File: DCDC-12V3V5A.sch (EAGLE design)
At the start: 37 parts, among them Q10 NMOSFET, Q9 NMOSFET, U1 LM3150MHX/NOPB

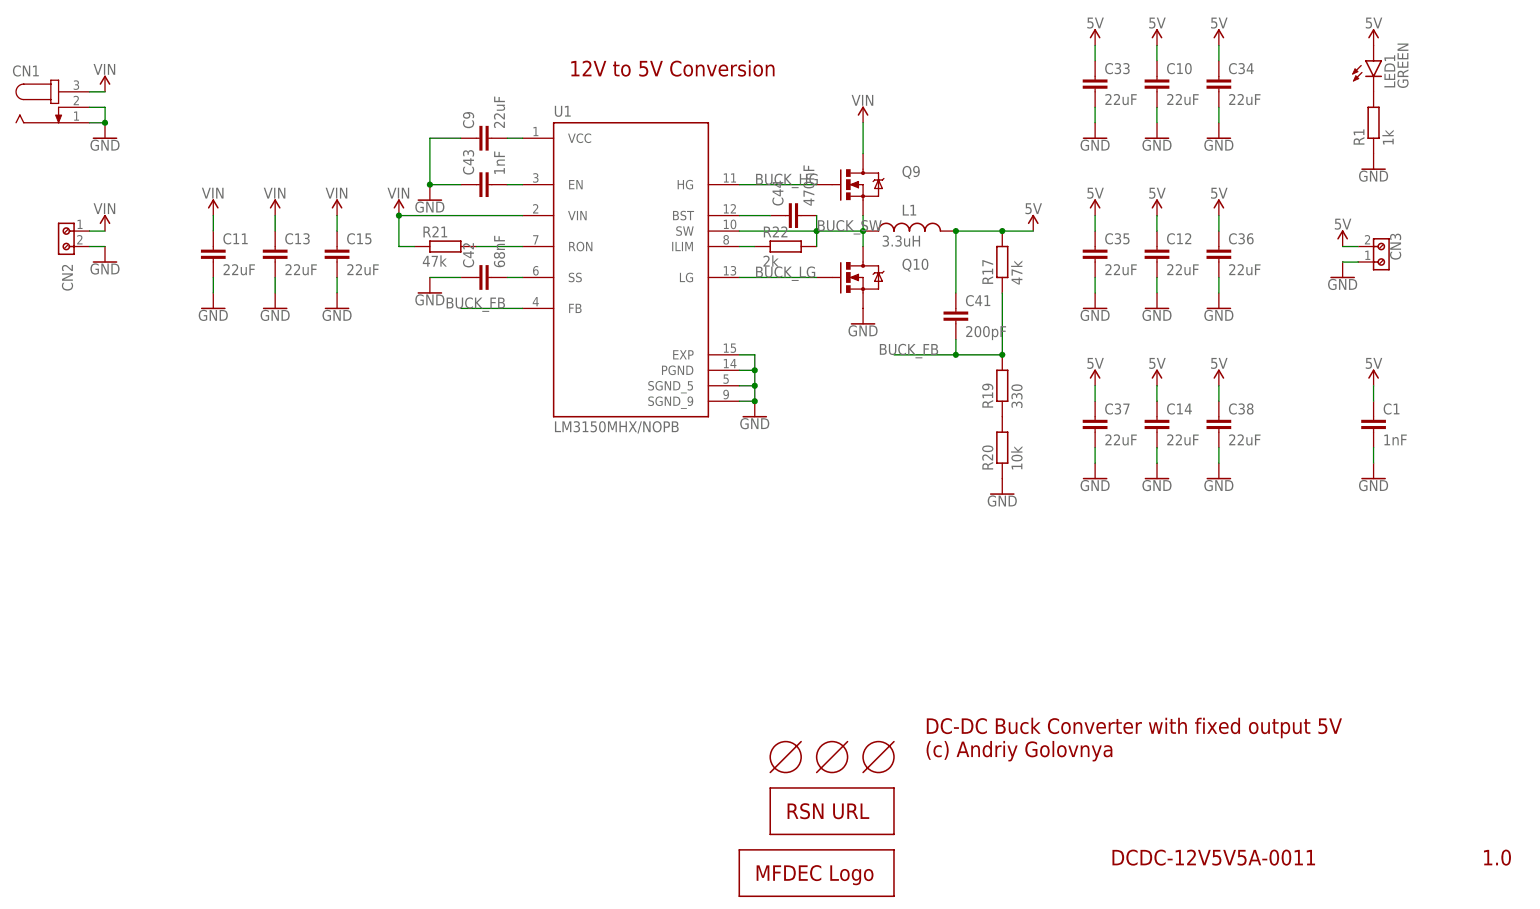
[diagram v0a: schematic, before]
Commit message: Fixed text on schematics. Generated PDF schematics. Removed wrongly committed CSV file.
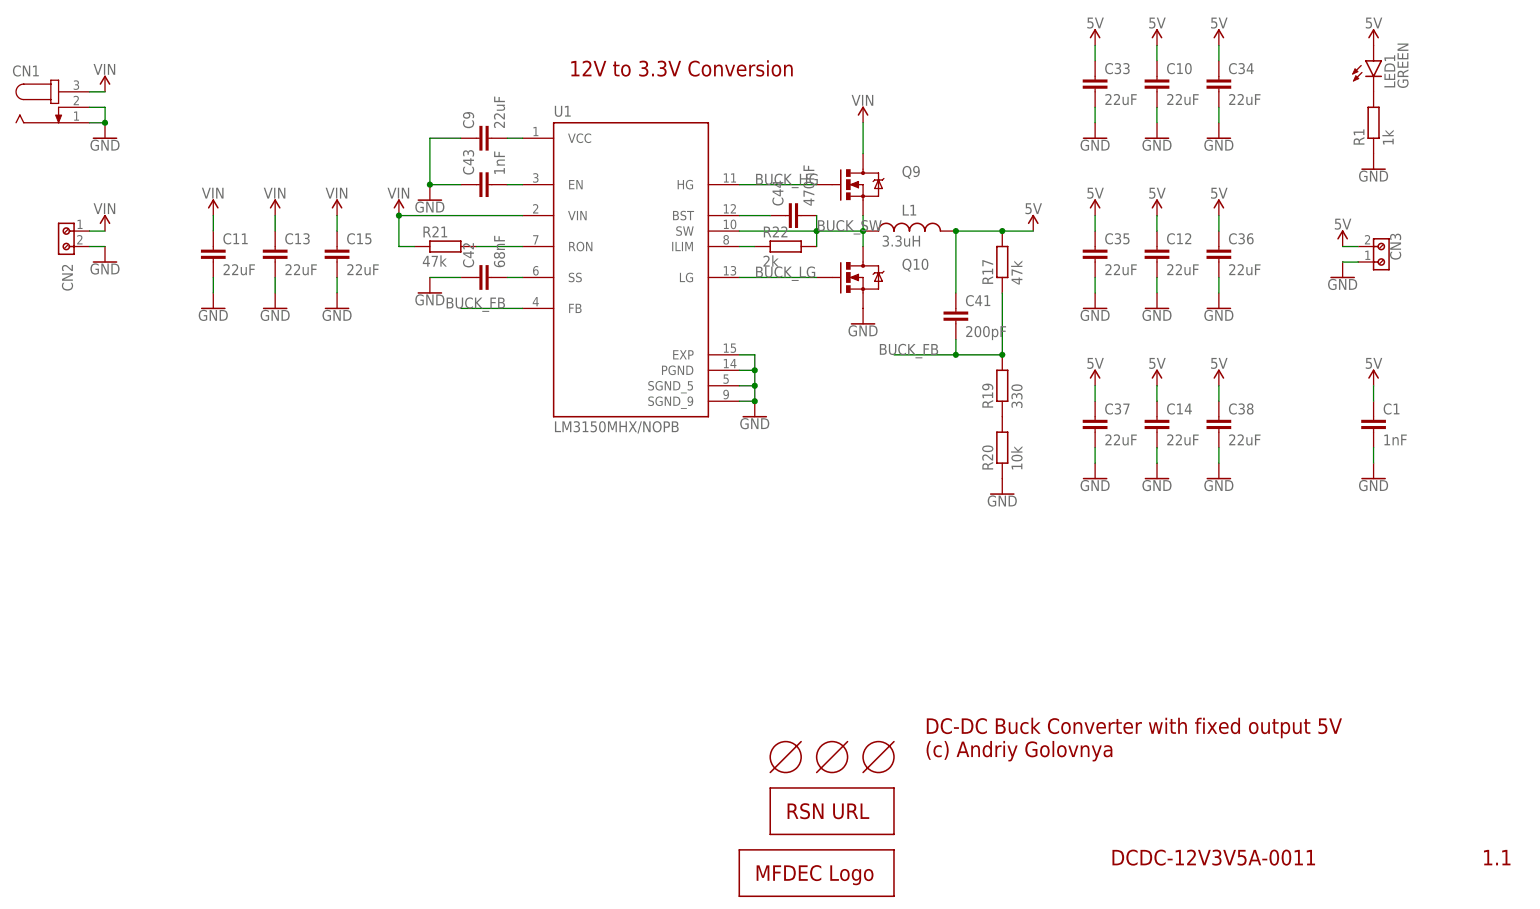
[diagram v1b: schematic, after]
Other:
- note added: "1.1"
- note added: "12V to 3.3V Conversion"
- note added: "DCDC-12V3V5A-0011"
- note removed: "1.0"
- note removed: "12V to 5V Conversion"
- note removed: "DCDC-12V5V5A-0011"
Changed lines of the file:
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@@
 <sheet>
 <plain>
-<text x="256.54" y="7.62" size="2.54" layer="94">1.0</text>
-<text x="195.58" y="7.62" size="2.54" layer="94">DCDC-12V5V5A-0011</text>
+<text x="256.54" y="7.62" size="2.54" layer="94">1.1</text>
+<text x="195.58" y="7.62" size="2.54" layer="94">DCDC-12V3V5A-0011</text>
 <text x="165.1" y="25.4" size="2.54" layer="94">DC-DC Buck Converter with fixed output 5V
 (c) Andriy Golovnya</text>
-<text x="106.68" y="137.16" size="2.54" layer="94">12V to 5V Conversion</text>
+<text x="106.68" y="137.16" size="2.54" layer="94">12V to 3.3V Conversion</text>
 </plain>
 <instances>

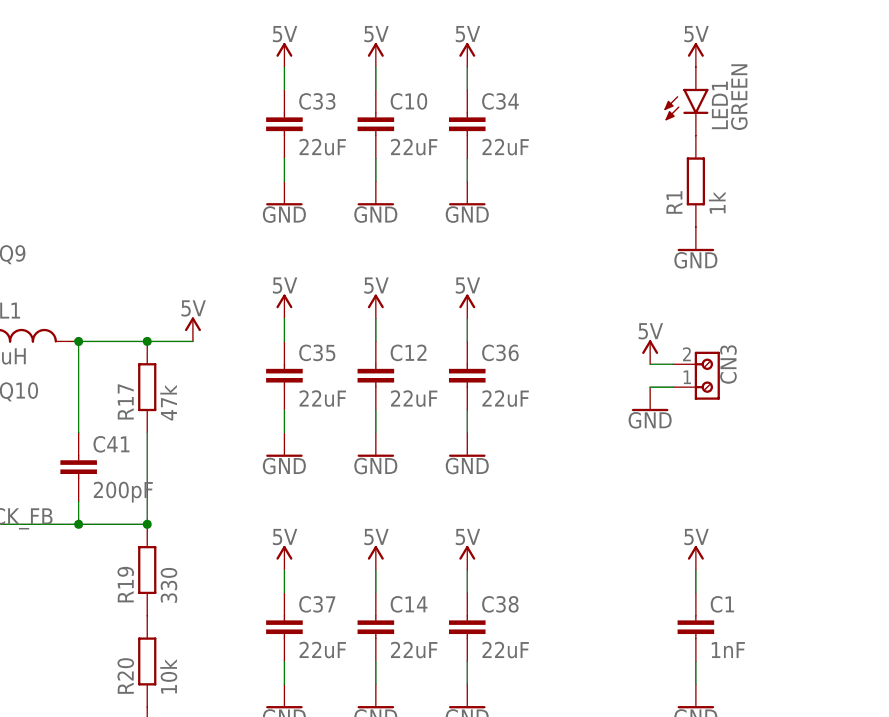
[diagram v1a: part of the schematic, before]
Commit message: Added proper voltage symbols on 3.3v and 12v boards. Generated PDF schematics.
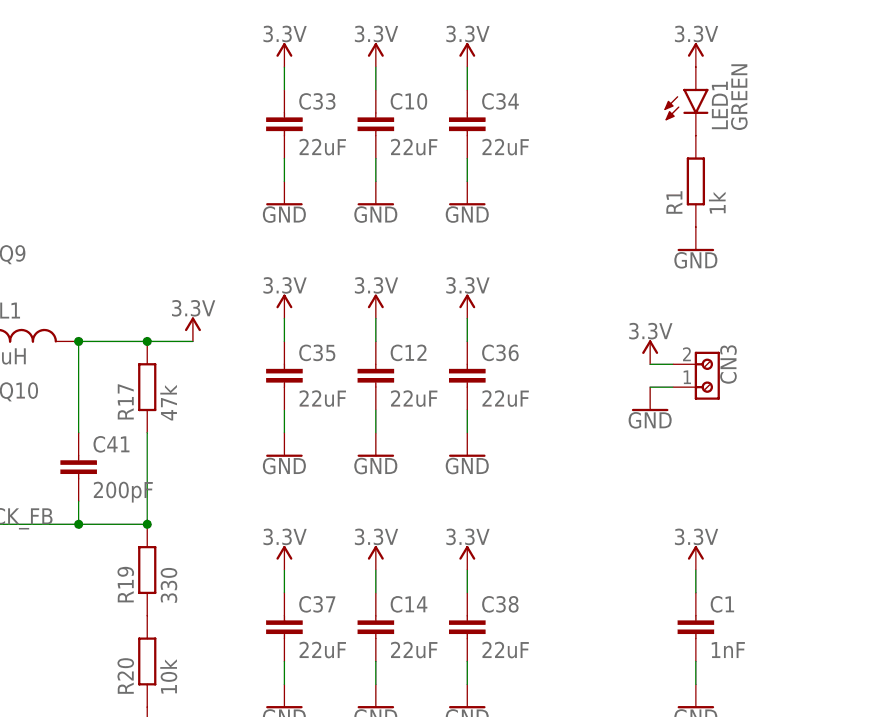
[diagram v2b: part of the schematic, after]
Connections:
- net 5V renamed 3.3V
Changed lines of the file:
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@@
 <part name="C37" library="rcl" library_urn="urn:adsk.eagle:library:334" deviceset="C-EU" device="C0805K" package3d_urn="urn:adsk.eagle:package:23681/2" value="22uF"/>
 <part name="C38" library="rcl" library_urn="urn:adsk.eagle:library:334" deviceset="C-EU" device="C0805K" package3d_urn="urn:adsk.eagle:package:23681/2" value="22uF"/>
-<part name="SUPPLY41" library="SparkFun-PowerSymbols" library_urn="urn:adsk.eagle:library:530" deviceset="5V" device=""/>
-<part name="SUPPLY42" library="SparkFun-PowerSymbols" library_urn="urn:adsk.eagle:library:530" deviceset="5V" device=""/>
-<part name="SUPPLY43" library="SparkFun-PowerSymbols" library_urn="urn:adsk.eagle:library:530" deviceset="5V" device=""/>
+<part name="SUPPLY41" library="SparkFun-PowerSymbols" library_urn="urn:adsk.eagle:library:530" deviceset="3.3V" device=""/>
+<part name="SUPPLY42" library="SparkFun-PowerSymbols" library_urn="urn:adsk.eagle:library:530" deviceset="3.3V" device=""/>
+<part name="SUPPLY43" library="SparkFun-PowerSymbols" library_urn="urn:adsk.eagle:library:530" deviceset="3.3V" device=""/>
 <part name="U1" library="LM3150MHX_NOPB" deviceset="LM3150MHX/NOPB" device=""/>
 <part name="Q9" library="BeagleBone_Blue_R3" library_urn="urn:adsk.eagle:library:5828899" deviceset="MOSFET-NCHANNEL" device="FDD8780" package3d_urn="urn:adsk.eagle:package:5829549/1" value="NMOSFET"/>
@@
 <part name="GND51" library="SparkFun-PowerSymbols" library_urn="urn:adsk.eagle:library:530" deviceset="GND" device=""/>
 <part name="L1" library="Wurth_Automotive_WE-CHSA" library_urn="urn:adsk.eagle:library:14076700" deviceset="WE-CHSA_1011" device="" package3d_urn="urn:adsk.eagle:package:13154812/4" technology="_7843330330" value="3.3uH"/>
-<part name="SUPPLY45" library="SparkFun-PowerSymbols" library_urn="urn:adsk.eagle:library:530" deviceset="5V" device=""/>
+<part name="SUPPLY45" library="SparkFun-PowerSymbols" library_urn="urn:adsk.eagle:library:530" deviceset="3.3V" device=""/>
 <part name="GND52" library="SparkFun-PowerSymbols" library_urn="urn:adsk.eagle:library:530" deviceset="GND" device=""/>
 <part name="SUPPLY46" library="SparkFun-PowerSymbols" library_urn="urn:adsk.eagle:library:530" deviceset="VIN" device=""/>
@@
 <part name="SUPPLY3" library="SparkFun-PowerSymbols" library_urn="urn:adsk.eagle:library:530" deviceset="VIN" device=""/>
 <part name="SUPPLY5" library="SparkFun-PowerSymbols" library_urn="urn:adsk.eagle:library:530" deviceset="VIN" device=""/>
-<part name="SUPPLY8" library="SparkFun-PowerSymbols" library_urn="urn:adsk.eagle:library:530" deviceset="5V" device=""/>
-<part name="SUPPLY47" library="SparkFun-PowerSymbols" library_urn="urn:adsk.eagle:library:530" deviceset="5V" device=""/>
-<part name="SUPPLY48" library="SparkFun-PowerSymbols" library_urn="urn:adsk.eagle:library:530" deviceset="5V" device=""/>
-<part name="SUPPLY49" library="SparkFun-PowerSymbols" library_urn="urn:adsk.eagle:library:530" deviceset="5V" device=""/>
-<part name="SUPPLY50" library="SparkFun-PowerSymbols" library_urn="urn:adsk.eagle:library:530" deviceset="5V" device=""/>
-<part name="SUPPLY51" library="SparkFun-PowerSymbols" library_urn="urn:adsk.eagle:library:530" deviceset="5V" device=""/>
+<part name="SUPPLY8" library="SparkFun-PowerSymbols" library_urn="urn:adsk.eagle:library:530" deviceset="3.3V" device=""/>
+<part name="SUPPLY47" library="SparkFun-PowerSymbols" library_urn="urn:adsk.eagle:library:530" deviceset="3.3V" device=""/>
+<part name="SUPPLY48" library="SparkFun-PowerSymbols" library_urn="urn:adsk.eagle:library:530" deviceset="3.3V" device=""/>
+<part name="SUPPLY49" library="SparkFun-PowerSymbols" library_urn="urn:adsk.eagle:library:530" deviceset="3.3V" device=""/>
+<part name="SUPPLY50" library="SparkFun-PowerSymbols" library_urn="urn:adsk.eagle:library:530" deviceset="3.3V" device=""/>
+<part name="SUPPLY51" library="SparkFun-PowerSymbols" library_urn="urn:adsk.eagle:library:530" deviceset="3.3V" device=""/>
 <part name="GND58" library="SparkFun-PowerSymbols" library_urn="urn:adsk.eagle:library:530" deviceset="GND" device=""/>
 <part name="GND59" library="SparkFun-PowerSymbols" library_urn="urn:adsk.eagle:library:530" deviceset="GND" device=""/>
@@
 <part name="SUPPLY1" library="SparkFun-PowerSymbols" library_urn="urn:adsk.eagle:library:530" deviceset="VIN" device=""/>
 <part name="GND3" library="SparkFun-PowerSymbols" library_urn="urn:adsk.eagle:library:530" deviceset="GND" device=""/>
-<part name="SUPPLY6" library="SparkFun-PowerSymbols" library_urn="urn:adsk.eagle:library:530" deviceset="5V" device=""/>
+<part name="SUPPLY6" library="SparkFun-PowerSymbols" library_urn="urn:adsk.eagle:library:530" deviceset="3.3V" device=""/>
 <part name="LOGO1" library="_my_logos" deviceset="RSNURL" device="_QR_8MM" value="RSNURL_QR_8MM"/>
 <part name="LOGO2" library="_my_logos" deviceset="MFDECLOGO" device="_L_10MM" value="MFDECLOGO_L_10MM"/>
 <part name="LED1" library="led" library_urn="urn:adsk.eagle:library:259" deviceset="LED" device="SML0603" package3d_urn="urn:adsk.eagle:package:15832/1" value="GREEN"/>
 <part name="R1" library="rcl" library_urn="urn:adsk.eagle:library:334" deviceset="R-EU_" device="R0603" package3d_urn="urn:adsk.eagle:package:23555/3" value="1k"/>
-<part name="SUPPLY7" library="SparkFun-PowerSymbols" library_urn="urn:adsk.eagle:library:530" deviceset="5V" device=""/>
+<part name="SUPPLY7" library="SparkFun-PowerSymbols" library_urn="urn:adsk.eagle:library:530" deviceset="3.3V" device=""/>
 <part name="GND4" library="SparkFun-PowerSymbols" library_urn="urn:adsk.eagle:library:530" deviceset="GND" device=""/>
 <part name="HOLE1" library="_my_fiducia" deviceset="TOOLINGHOLE" device=""/>
@@
 <part name="HOLE3" library="_my_fiducia" deviceset="TOOLINGHOLE" device=""/>
 <part name="C1" library="rcl" library_urn="urn:adsk.eagle:library:334" deviceset="C-EU" device="C0603K" package3d_urn="urn:adsk.eagle:package:23680/2" value="1nF"/>
-<part name="SUPPLY9" library="SparkFun-PowerSymbols" library_urn="urn:adsk.eagle:library:530" deviceset="5V" device=""/>
+<part name="SUPPLY9" library="SparkFun-PowerSymbols" library_urn="urn:adsk.eagle:library:530" deviceset="3.3V" device=""/>
 <part name="GND5" library="SparkFun-PowerSymbols" library_urn="urn:adsk.eagle:library:530" deviceset="GND" device=""/>
 <part name="SUPPLY4" library="SparkFun-PowerSymbols" library_urn="urn:adsk.eagle:library:530" deviceset="VIN" device=""/>
@@
 </segment>
 </net>
-<net name="5V" class="0">
+<net name="3.3V" class="0">
 <segment>
 <pinref part="C34" gate="G$1" pin="1"/>
 <wire x1="213.36" y1="139.7" x2="213.36" y2="142.24" width="0.1524" layer="91"/>
-<pinref part="SUPPLY43" gate="G$1" pin="5V"/>
+<pinref part="SUPPLY43" gate="G$1" pin="3.3V"/>
 </segment>
 <segment>
 <pinref part="C36" gate="G$1" pin="1"/>
 <wire x1="213.36" y1="111.76" x2="213.36" y2="114.3" width="0.1524" layer="91"/>
-<pinref part="SUPPLY42" gate="G$1" pin="5V"/>
+<pinref part="SUPPLY42" gate="G$1" pin="3.3V"/>
 </segment>
 <segment>
 <pinref part="C38" gate="G$1" pin="1"/>
 <wire x1="213.36" y1="83.82" x2="213.36" y2="86.36" width="0.1524" layer="91"/>
-<pinref part="SUPPLY41" gate="G$1" pin="5V"/>
+<pinref part="SUPPLY41" gate="G$1" pin="3.3V"/>
 </segment>
 <segment>
 <pinref part="L1" gate="G$1" pin="2"/>
-<pinref part="SUPPLY45" gate="G$1" pin="5V"/>
+<pinref part="SUPPLY45" gate="G$1" pin="3.3V"/>
 <pinref part="R17" gate="G$1" pin="2"/>
 <wire x1="170.18" y1="111.76" x2="177.8" y2="111.76" width="0.1524" layer="91"/>
@@
 <pinref part="C10" gate="G$1" pin="1"/>
 <wire x1="203.2" y1="142.24" x2="203.2" y2="139.7" width="0.1524" layer="91"/>
-<pinref part="SUPPLY8" gate="G$1" pin="5V"/>
+<pinref part="SUPPLY8" gate="G$1" pin="3.3V"/>
 </segment>
 <segment>
 <pinref part="C33" gate="G$1" pin="1"/>
 <wire x1="193.04" y1="142.24" x2="193.04" y2="139.7" width="0.1524" layer="91"/>
-<pinref part="SUPPLY47" gate="G$1" pin="5V"/>
+<pinref part="SUPPLY47" gate="G$1" pin="3.3V"/>
 </segment>
 <segment>
 <pinref part="C12" gate="G$1" pin="1"/>
 <wire x1="203.2" y1="114.3" x2="203.2" y2="111.76" width="0.1524" layer="91"/>
-<pinref part="SUPPLY48" gate="G$1" pin="5V"/>
+<pinref part="SUPPLY48" gate="G$1" pin="3.3V"/>
 </segment>
 <segment>
 <pinref part="C35" gate="G$1" pin="1"/>
 <wire x1="193.04" y1="114.3" x2="193.04" y2="111.76" width="0.1524" layer="91"/>
-<pinref part="SUPPLY49" gate="G$1" pin="5V"/>
+<pinref part="SUPPLY49" gate="G$1" pin="3.3V"/>
 </segment>
 <segment>
 <pinref part="C14" gate="G$1" pin="1"/>
 <wire x1="203.2" y1="86.36" x2="203.2" y2="83.82" width="0.1524" layer="91"/>
-<pinref part="SUPPLY50" gate="G$1" pin="5V"/>
+<pinref part="SUPPLY50" gate="G$1" pin="3.3V"/>
 </segment>
 <segment>
 <pinref part="C37" gate="G$1" pin="1"/>
 <wire x1="193.04" y1="86.36" x2="193.04" y2="83.82" width="0.1524" layer="91"/>
-<pinref part="SUPPLY51" gate="G$1" pin="5V"/>
-</segment>
-<segment>
-<pinref part="SUPPLY6" gate="G$1" pin="5V"/>
+<pinref part="SUPPLY51" gate="G$1" pin="3.3V"/>
+</segment>
+<segment>
+<pinref part="SUPPLY6" gate="G$1" pin="3.3V"/>
 <pinref part="CN3" gate="G$1" pin="2"/>
 <wire x1="233.68" y1="109.22" x2="236.22" y2="109.22" width="0.1524" layer="91"/>
@@
 <segment>
 <pinref part="LED1" gate="G$1" pin="A"/>
-<pinref part="SUPPLY7" gate="G$1" pin="5V"/>
+<pinref part="SUPPLY7" gate="G$1" pin="3.3V"/>
 </segment>
 <segment>
 <pinref part="C1" gate="G$1" pin="1"/>
-<pinref part="SUPPLY9" gate="G$1" pin="5V"/>
+<pinref part="SUPPLY9" gate="G$1" pin="3.3V"/>
 <wire x1="238.76" y1="83.82" x2="238.76" y2="86.36" width="0.1524" layer="91"/>
 </segment>

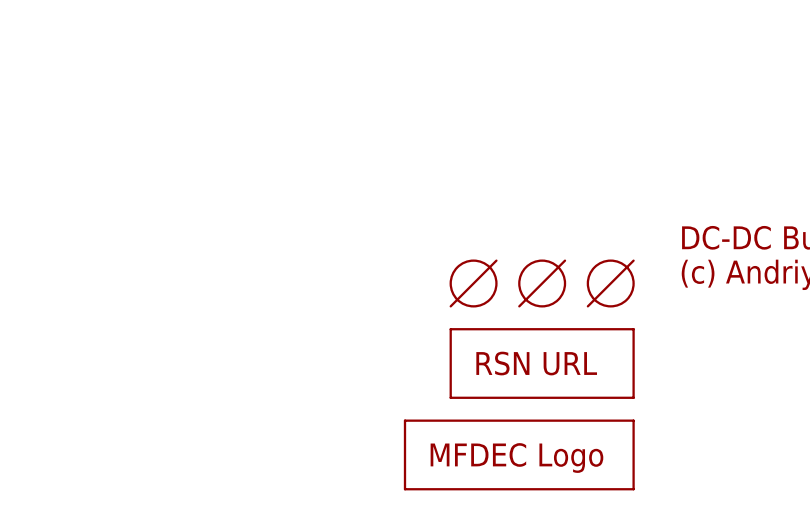
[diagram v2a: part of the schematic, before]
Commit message: Moved some texts and tooling holes a bit. Generated CAM files. Generated PNG preview. Generated PDF schematics. Renamed BoM and PnP files.
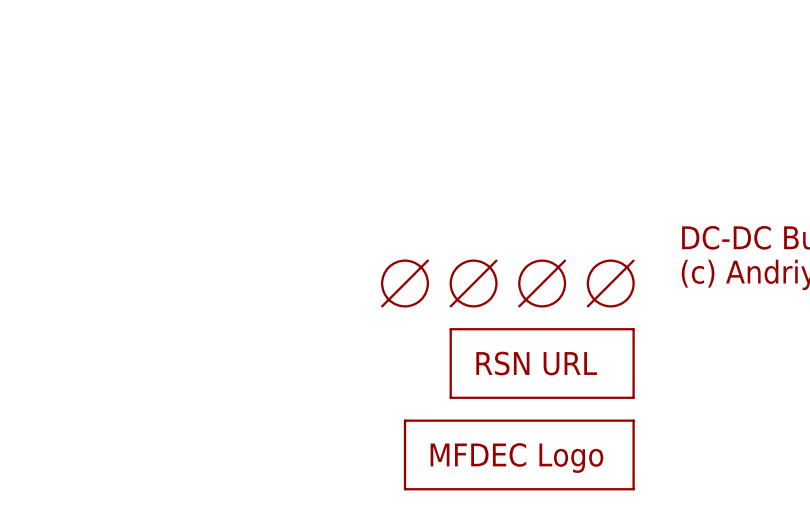
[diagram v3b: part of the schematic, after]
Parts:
- added HOLE4: TOOLINGHOLE, _my_fiducia:TOOLINGHOLE
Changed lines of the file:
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@@
 <part name="SUPPLY4" library="SparkFun-PowerSymbols" library_urn="urn:adsk.eagle:library:530" deviceset="VIN" device=""/>
 <part name="GND1" library="SparkFun-PowerSymbols" library_urn="urn:adsk.eagle:library:530" deviceset="GND" device=""/>
+<part name="HOLE4" library="_my_fiducia" deviceset="TOOLINGHOLE" device=""/>
 </parts>
 <sheets>
@@
 <attribute name="VALUE" x="30.48" y="106.426" size="1.778" layer="96" align="top-center"/>
 </instance>
+<instance part="HOLE4" gate="G$1" x="134.62" y="25.4" smashed="yes"/>
 </instances>
 <busses>
